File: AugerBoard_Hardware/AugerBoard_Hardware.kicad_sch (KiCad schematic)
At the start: 23 parts, among them J1 RJ45_LED_Shielded, U1 Teensy4.1_DEV-16771, U2 OKI-78SR-5_1.5-W36H-C

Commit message: Demonstration of push and pulling and commiting
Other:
- note added: "LED"
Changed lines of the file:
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@@
+		)
+	)
+	(text "LED"
+		(exclude_from_sim no)
+		(at 85.598 190.246 0)
+		(effects
+			(font
+				(size 5.08 5.08)
+			)
 		)
 	)

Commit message: Added temp and humidity, direction switch, test buttons, and leds
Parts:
- added Conn6, Conn7: Molex_SL_02, symbol MRDT_Connectors:Molex_SL_02
- added D4: Blue, symbol Device:LED
- added R6: 30, symbol Device:R
- added R7: 50k, symbol Device:R
- added R8: 25, symbol Device:R
- added SW1: SW_SPDT, symbol Switch:SW_SPDT
- added SW2, SW3: SW_Push, symbol Switch:SW_Push
- D1, D2, D3: value LED -> Green
- R1, R2: value 4700 -> 4.7k
- R3: value R -> 300
- R4: value R -> 560
- R5: value R -> 2.2k
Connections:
- net +12V: now also R5.1
- net +3.3V: now also R3.1, R6.2, SW1.1 (A)
- net +5V: now also R4.1, R7.1, R8.1
- net GND: now also D1.1 (K), D2.1 (K), D3.1 (K), Conn6.2, Conn7.2, SW1.3 (C), SW2.2, SW3.2
- net at D1.2 (A): now also R3.2
- net at D2.2 (A): now also R4.2
- net at D3.2 (A): now also R5.2
- new net: D4.2 (A), R6.1
- new net Dir_Switch: D4.1 (K), SW1.2 (B)
- new net Humidity: Conn6.1, R7.2
- new net SW1: SW2.1
- new net SW2: SW3.1
- new net Temp: Conn7.1, R8.2
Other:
- note added: "Direction Switch"
- note added: "Humidity and Temp Sensors"
- note added: "LEDs"
- note added: "Test Buttons"
- note removed: "LED"
- moved on the sheet: C1, Conn2, Conn3, Conn4, Conn5, D1, D2, D3, J1, R1, R2, R3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

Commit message: Added temp/humidity, switches and buttons, leds, and moco stuff
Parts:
- added Conn10, Conn11: Molex_SL_02, symbol MRDT_Connectors:Molex_SL_02
- added Conn8: AndersonPP, symbol MRDT_Connectors:AndersonPP
- added Conn9: Molex_SL_05, symbol MRDT_Connectors:Molex_SL_05
- added R10, R9: 4.7k, symbol Device:R
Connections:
- net +12V: now also Conn8.2 (V+Log)
- net +3.3V: now also Conn10.1, Conn11.1
- net Dir_Switch: now also U1.18 (A4)
- net Encoder_1a: now also U1.14 (A0)
- net Encoder_1b: now also U1.15 (A1)
- net Encoder_2a: now also U1.16 (A2)
- net Encoder_2b: now also U1.17 (A3)
- net GND: now also Conn8.1 (GND), R10.1, R9.1
- net Humidity: now also U1.22 (A8)
- net LimitSwitch1: now also U1.0 (RX1)
- net LimitSwitch2: now also U1.1 (TX1)
- net SW1: now also U1.29 (TX7)
- net SW2: now also U1.34 (RX8)
- net Temp: now also U1.21 (A7)
- net LimitSwitch3: now reaches U1.7 (RX2)
- net LimitSwitch3: now also Conn10.2, R9.2
- net LimitSwitch4: now reaches U1.8 (TX2)
- net LimitSwitch4: now also Conn11.2, R10.2
- new net CS: Conn9.2
- new net IN_A: Conn9.3
- new net IN_B: Conn9.4
- new net PWM: Conn9.5
- new net SEL: Conn9.1
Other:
- note added: "Teensy 4.1"
- moved on the sheet: C2, C3, C4, C5, C6, C7, Conn1A, Conn1B, Conn4, Conn5, D1, D2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

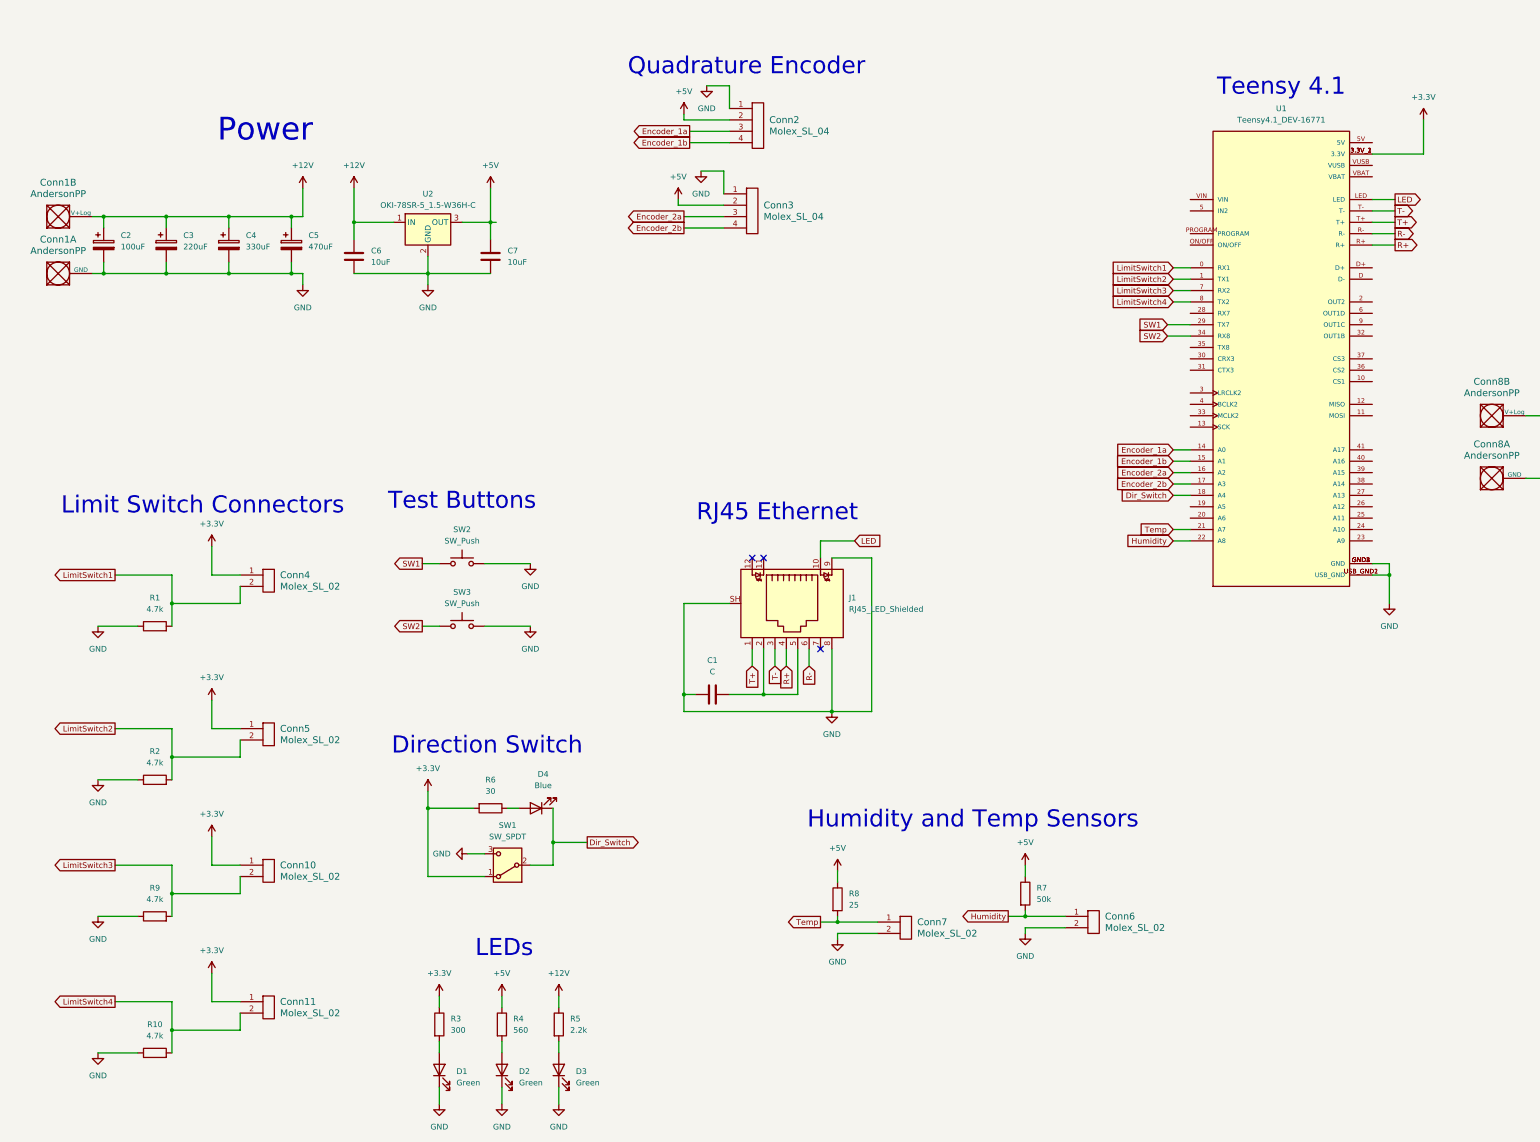
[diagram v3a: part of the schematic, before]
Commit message: Organized and Added Stuff
Added two more test buttons. Previously we only had 2 and we have two motors so I assume that we need 2 for each motor forward and backward running.

Will looked at our test buttons and told me they won't work but they are the same as last years so I built the version he said would work. I'm confused though because last year had the same test button schematic.
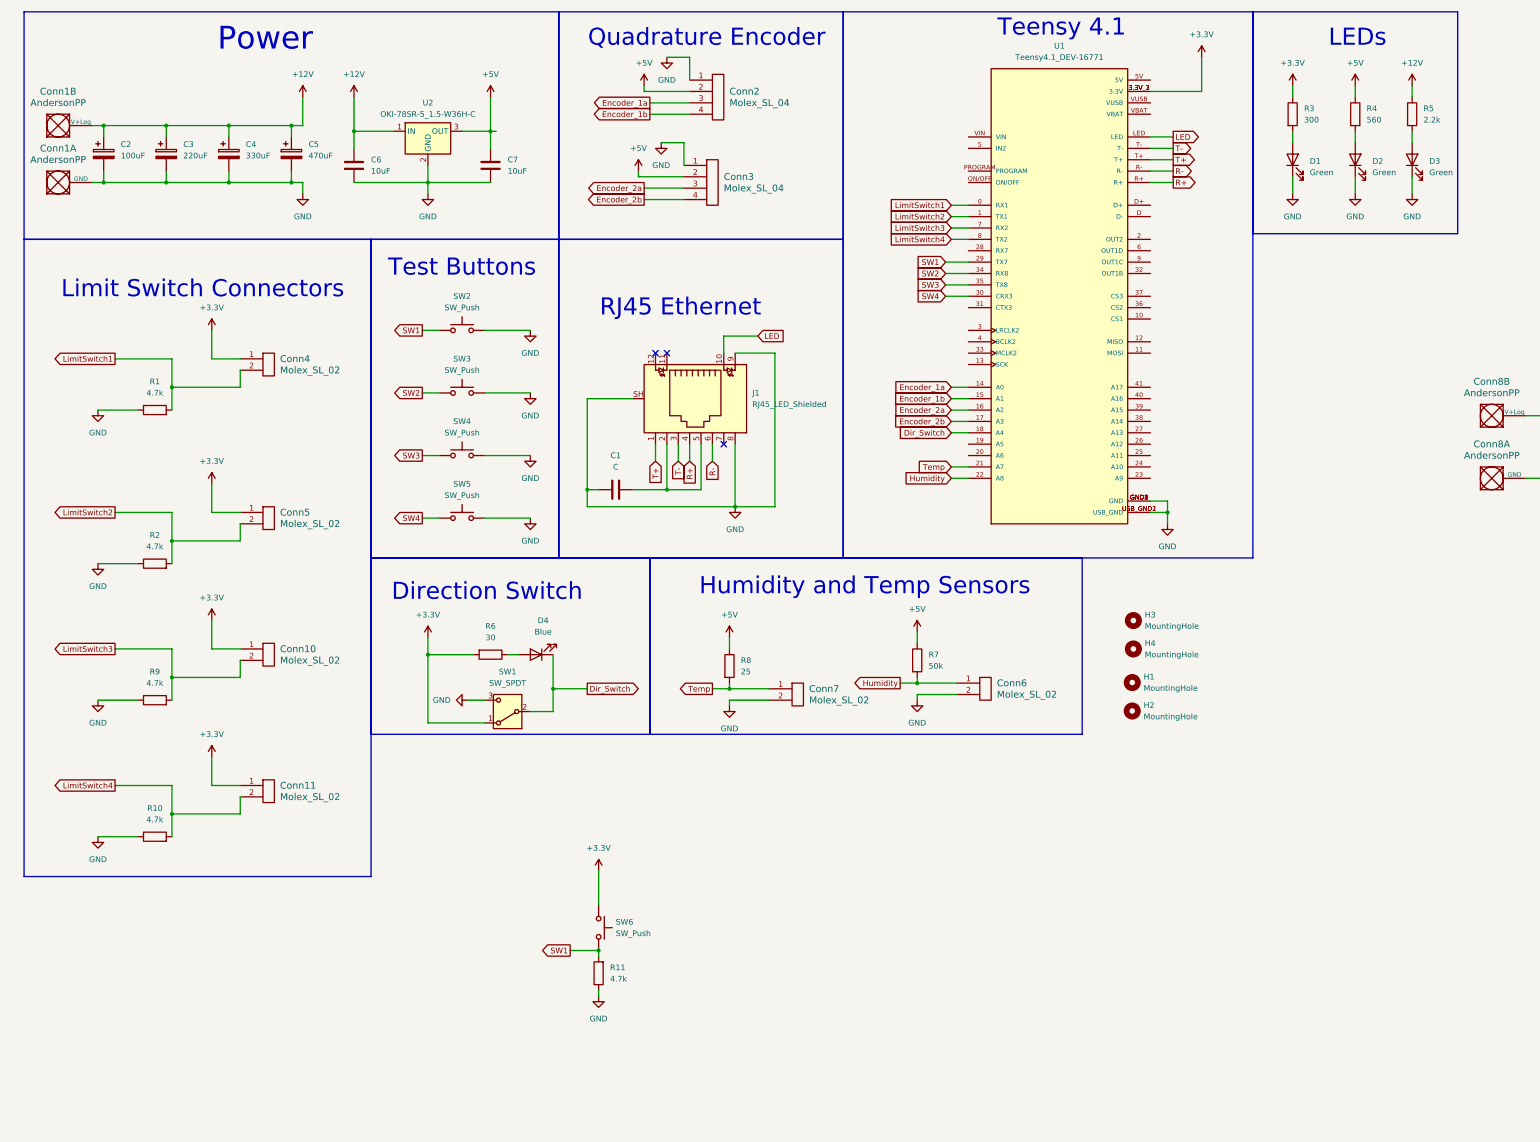
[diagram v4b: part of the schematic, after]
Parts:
- added H1, H2, H3, H4: MountingHole, MRDT_Drill_Holes:4_40_Hole_Corner, symbol Mechanical:MountingHole
- added R11: 4.7k, symbol Device:R
- added SW4, SW5, SW6: SW_Push, symbol Switch:SW_Push
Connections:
- net +3.3V: now also SW6.1
- net GND: now also R11.1, SW4.2, SW5.2
- net SW1: now also R11.2, SW6.2
- net SW4: now reaches U1.30 (CRX3)
- net SW4: now also SW5.1
- net SW3: now reaches U1.35 (TX8)
- net SW3: now also SW4.1
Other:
- moved on the sheet: C1, C2, C3, C4, C5, C6, C7, Conn10, Conn11, Conn1A, Conn1B, Conn2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

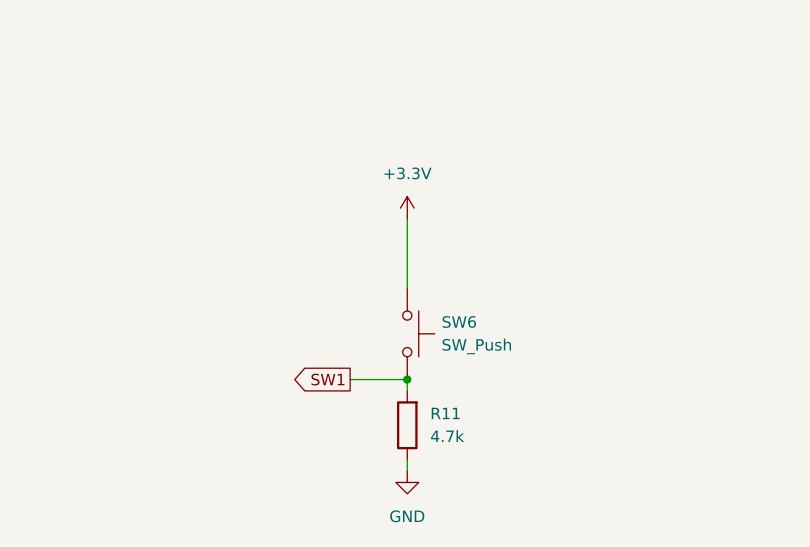
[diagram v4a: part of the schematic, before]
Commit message: Update to my previous comit
Will and I realized the buttons were fine because of teensy internal pullup
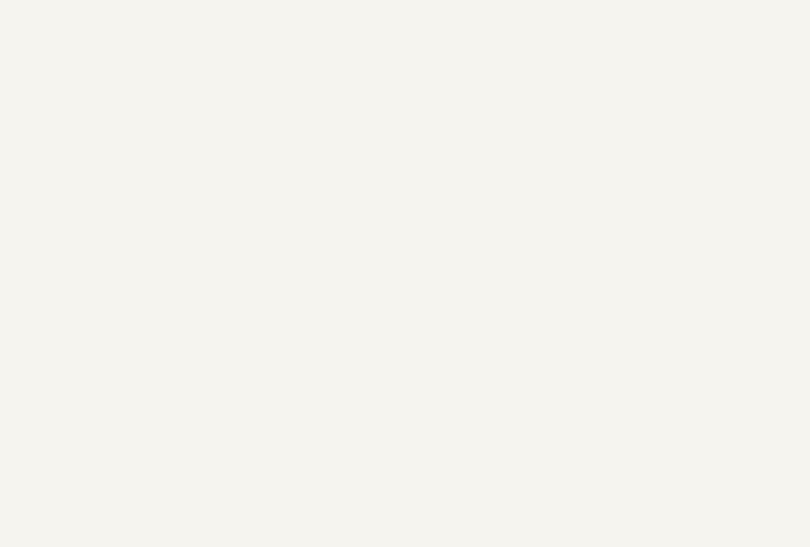
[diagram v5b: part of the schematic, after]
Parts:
- removed R11: 4.7k, symbol Device:R
- removed SW6: SW_Push, symbol Switch:SW_Push

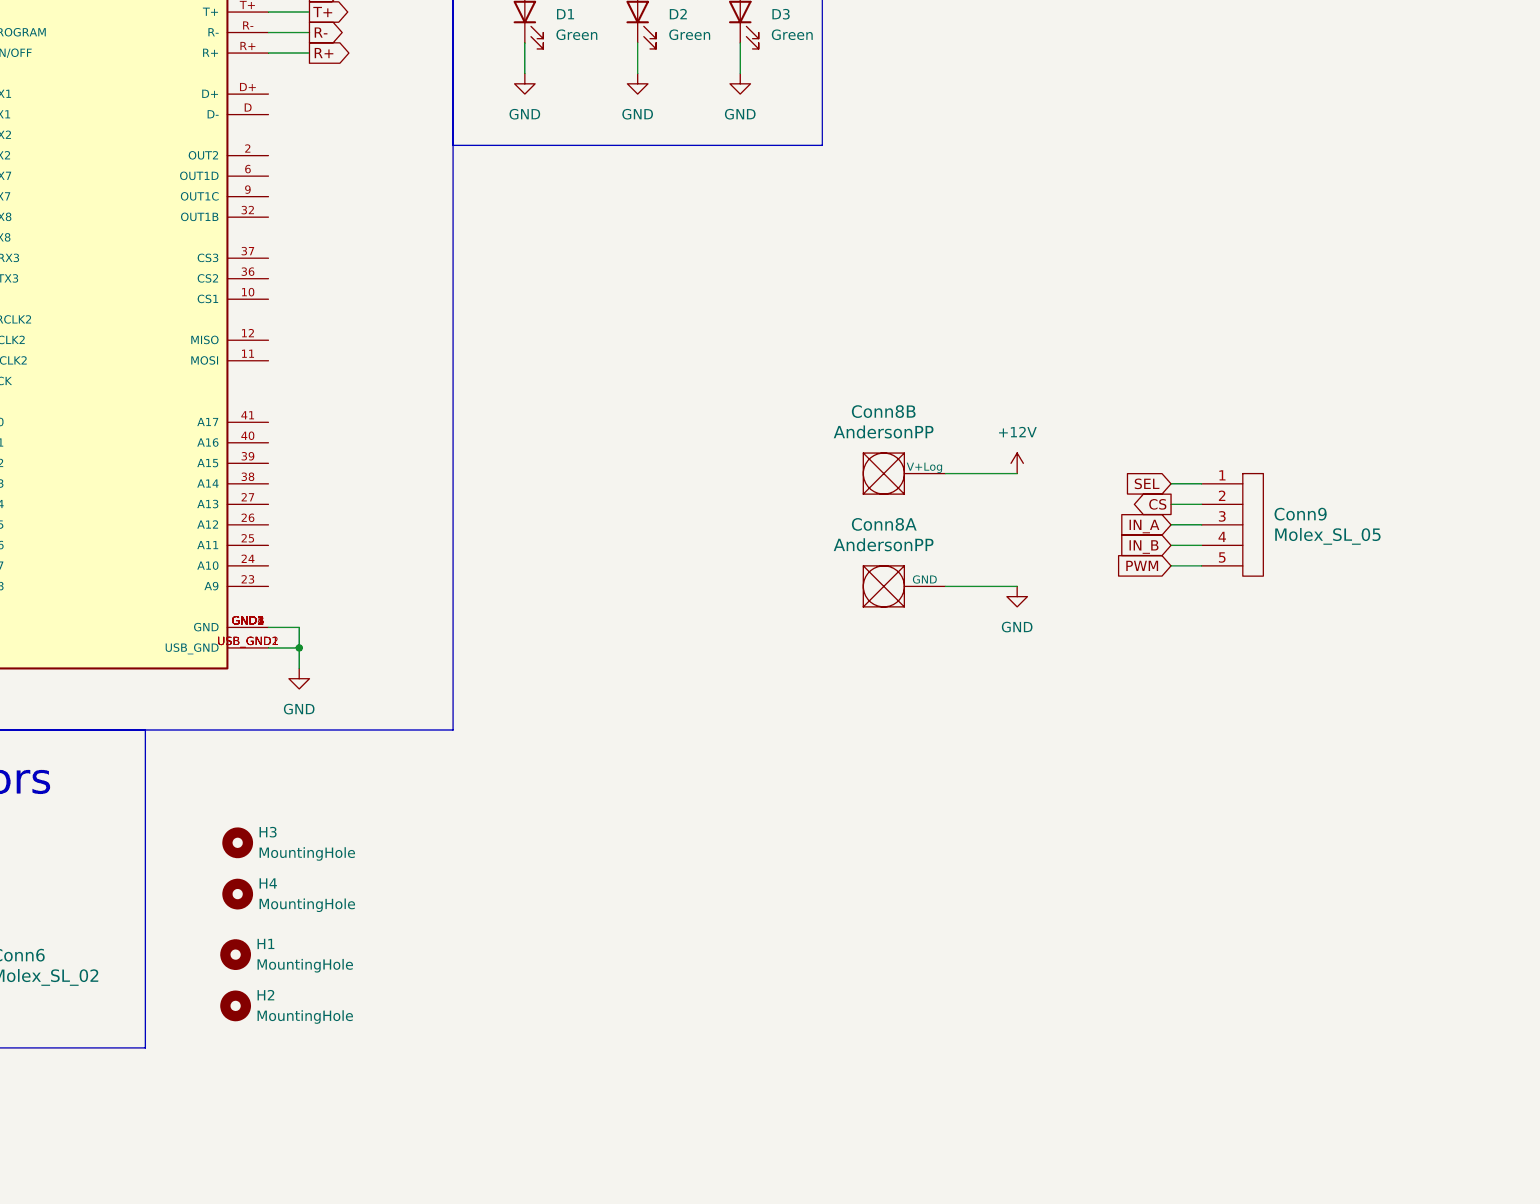
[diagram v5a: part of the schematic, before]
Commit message: Added 2 more dumb moco connections
-Still need to fix dumb moco pinouts
-double check all pinouts
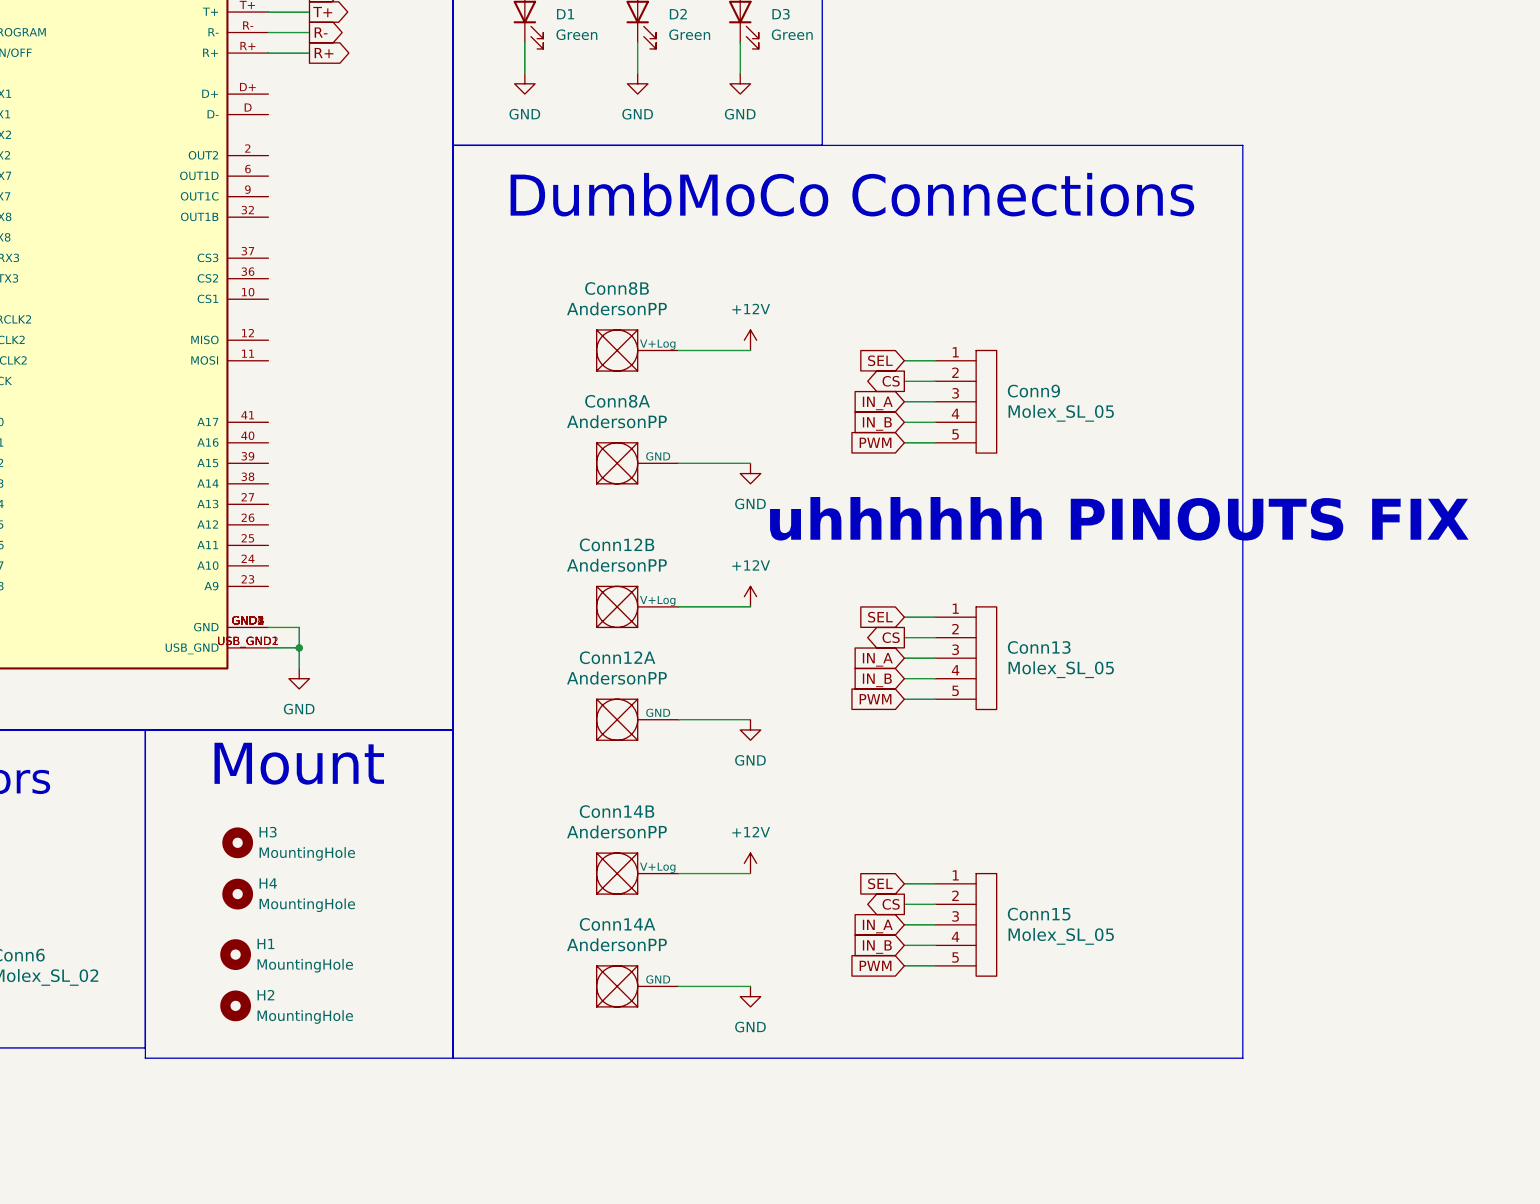
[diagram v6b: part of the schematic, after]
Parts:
- added Conn12, Conn14: AndersonPP, symbol MRDT_Connectors:AndersonPP
- added Conn13, Conn15: Molex_SL_05, symbol MRDT_Connectors:Molex_SL_05
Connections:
- net +12V: now also Conn12.2 (V+Log), Conn14.2 (V+Log)
- net CS: now also Conn13.2, Conn15.2
- net GND: now also Conn12.1 (GND), Conn14.1 (GND)
- net IN_A: now also Conn13.3, Conn15.3
- net IN_B: now also Conn13.4, Conn15.4
- net PWM: now also Conn13.5, Conn15.5
- net SEL: now also Conn13.1, Conn15.1
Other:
- note added: "DumbMoCo Connections"
- note added: "Mount"
- note added: "uhhhhhh PINOUTS FIX"
- moved on the sheet: Conn8A, Conn8B, Conn9
